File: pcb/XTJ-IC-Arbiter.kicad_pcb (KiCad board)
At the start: 2 copper layers, 80.2 x 67.8 mm, 56 parts, among them IC1 SN74LV125AN, J3 DTM13-12PA-R008, Q1 NPN, U1 LM2675N-5.0/NOPB, U2 CDP68HC68S1, U3 EEC-325X4A, U4 MCP2562-H-P, U5 SP723APP, U6 MCP1700-3302E/TO

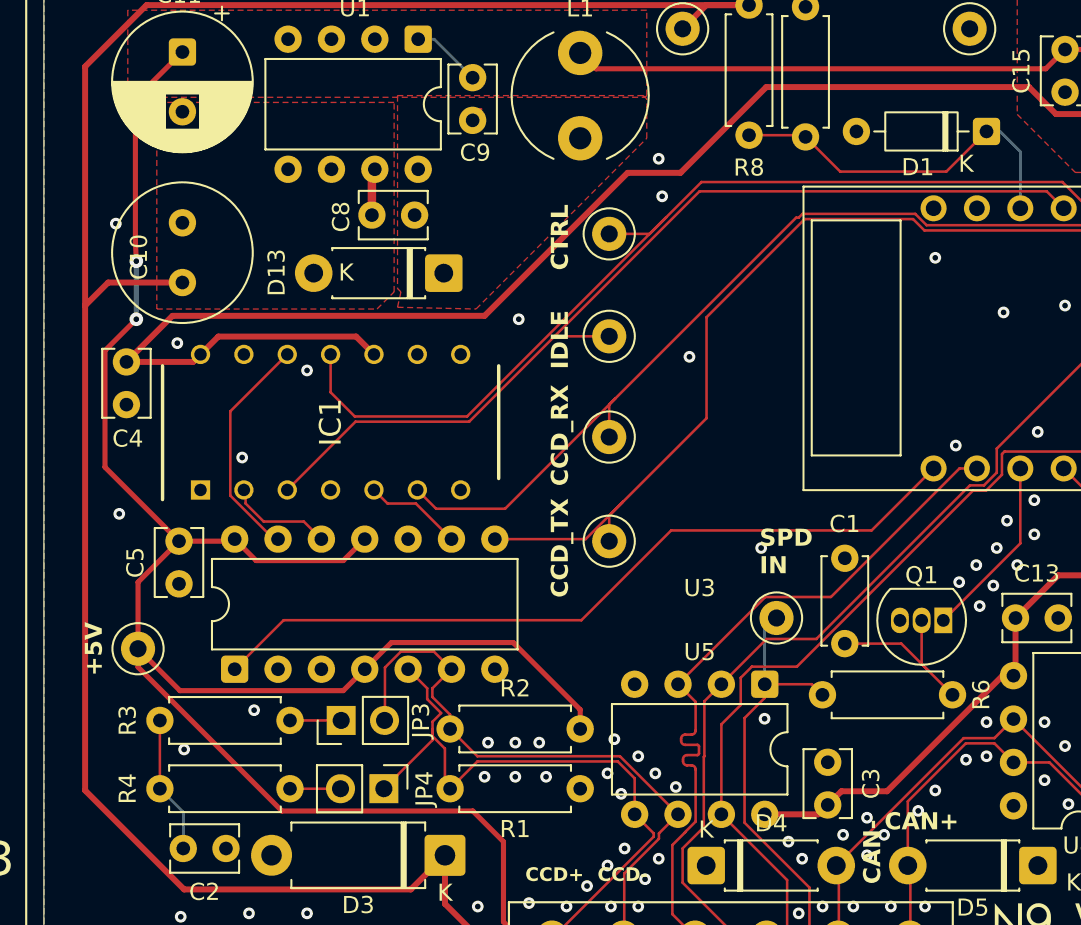
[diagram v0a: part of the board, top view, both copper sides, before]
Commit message: ensure ext I/Os are length tuned
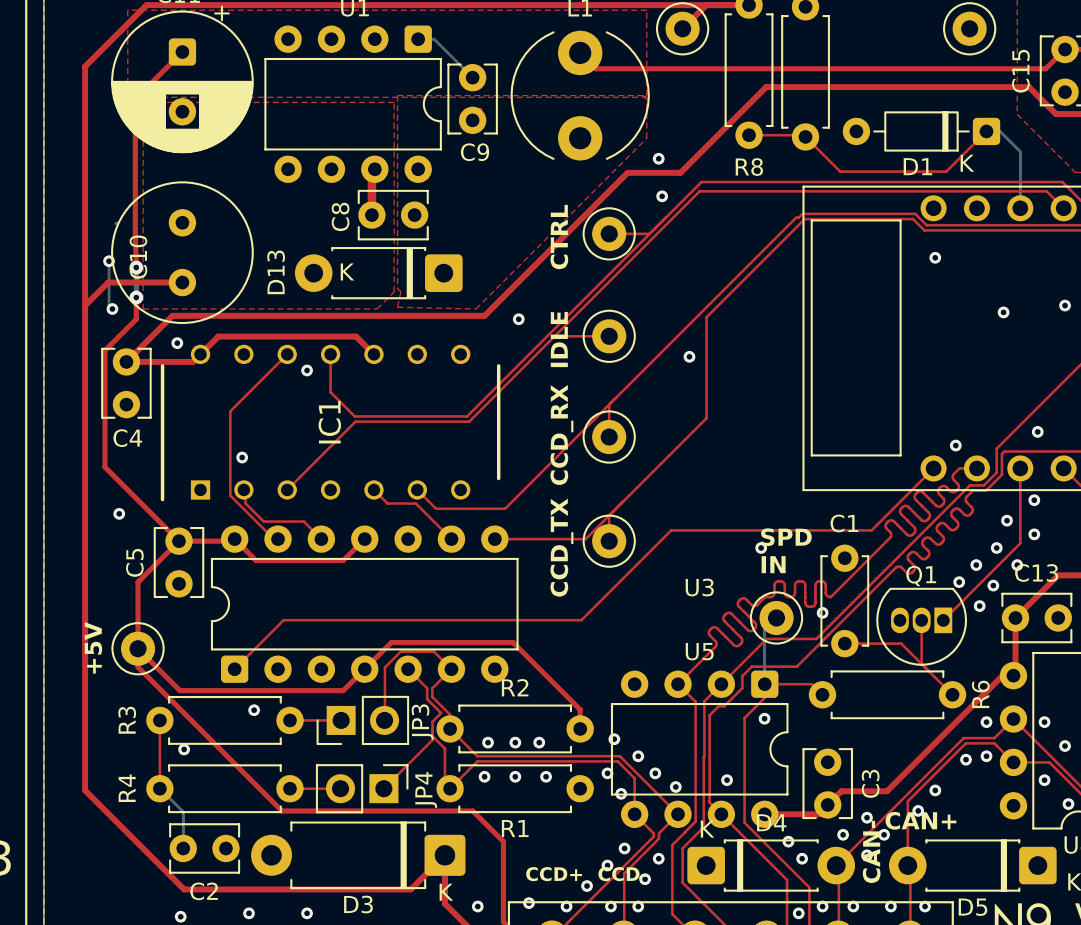
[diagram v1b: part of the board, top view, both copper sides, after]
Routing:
- net IO/1: track 41.9 -> 61.1 mm
- net IO/3: track 54.7 -> 62.0 mm
- net GND: track 0.07 -> 2.95 mm, vias 101 -> 104
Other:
- board text added: "Extended I/O pins: IO/1 -> Pin 18 IO/2 -> Pin 26 IO/3 -> Pin 4"
- board text removed: "Extended I/O pins: IO/1 -> Pin 26 IO/2 -> Pin 33 IO/3 -> Pin 18"

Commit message: After the 4 layer adventure, cleanup
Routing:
- net +5V: track 235.4 -> 235.5 mm, vias 3 -> 2
- net GND: vias 104 -> 0

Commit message: Hand tune the differential lengths (CAD/CCD)
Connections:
- net 12V_MEASURE renamed 12v_meter
- XA1 pad 13: IO/2 -> IO/1
- XA1 pad 2: IO/1 -> IO/2
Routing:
- net IO/2: track 61.4 -> 38.8 mm
- net IO/3: track 62.0 -> 55.5 mm
- net ccd-: track 36.1 -> 40.5 mm
- net +5V: track 235.5 -> 231.7 mm
- net ccd+: track 36.8 -> 39.9 mm
- net can-: track 36.1 -> 38.0 mm
- net can+: track 36.0 -> 37.7 mm
- net +3V3: track 149.2 -> 150.4 mm
- net GND: vias 0 -> 5

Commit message: silkscreen work
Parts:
- moved G*** 44.7 mm to (119.0, 121.0)
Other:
- board text added: "VOUT"
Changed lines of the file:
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@@
 	(footprint "parts:N9Works-Small"
 		(layer "F.Cu")
-		(at 163.574 117.200651)
+		(at 118.99245 121.000266)
 		(property "Reference" "G***"
 			(at 0 0 0)
@@
 	)
 	(gr_text "XJ/TJ CAN+CCD \nBus Arbiter v3.0\n"
-		(at 156 121.2 0)
+		(at 156.2 121 0)
 		(layer "F.SilkS")
 		(effects
@@
 		)
 	)
-	(gr_text "IO/1"
+	(gr_text "IO/3"
 		(at 142.646164 122.174 0)
 		(layer "B.SilkS")
@@
 		)
 	)
-	(gr_text "IO/3"
+	(gr_text "IO/1"
 		(at 138.684 116.332 0)
 		(layer "B.SilkS")
@@
 	(gr_text "CAN+"
 		(at 151.13 116.332 0)
+		(layer "B.SilkS")
+		(effects
+			(font
+				(size 1 1)
+				(thickness 0.15)
+			)
+			(justify mirror)
+		)
+	)
+	(gr_text "VOUT"
+		(at 138.6 122.2 0)
 		(layer "B.SilkS")
 		(effects
@@
 		)
 	)
+	(gr_text "+12V"
+		(at 134.8 126.6 0)
+		(layer "B.SilkS")
+		(effects
+			(font
+				(size 1 1)
+				(thickness 0.15)
+			)
+			(justify mirror)
+		)
+	)
 	(gr_text "CAN-"
 		(at 146.558 116.332 0)
@@
 	)
 	(gr_text "+5V"
-		(at 138.938 122.174 0)
+		(at 139 126.6 0)
 		(layer "B.SilkS")
 		(effects

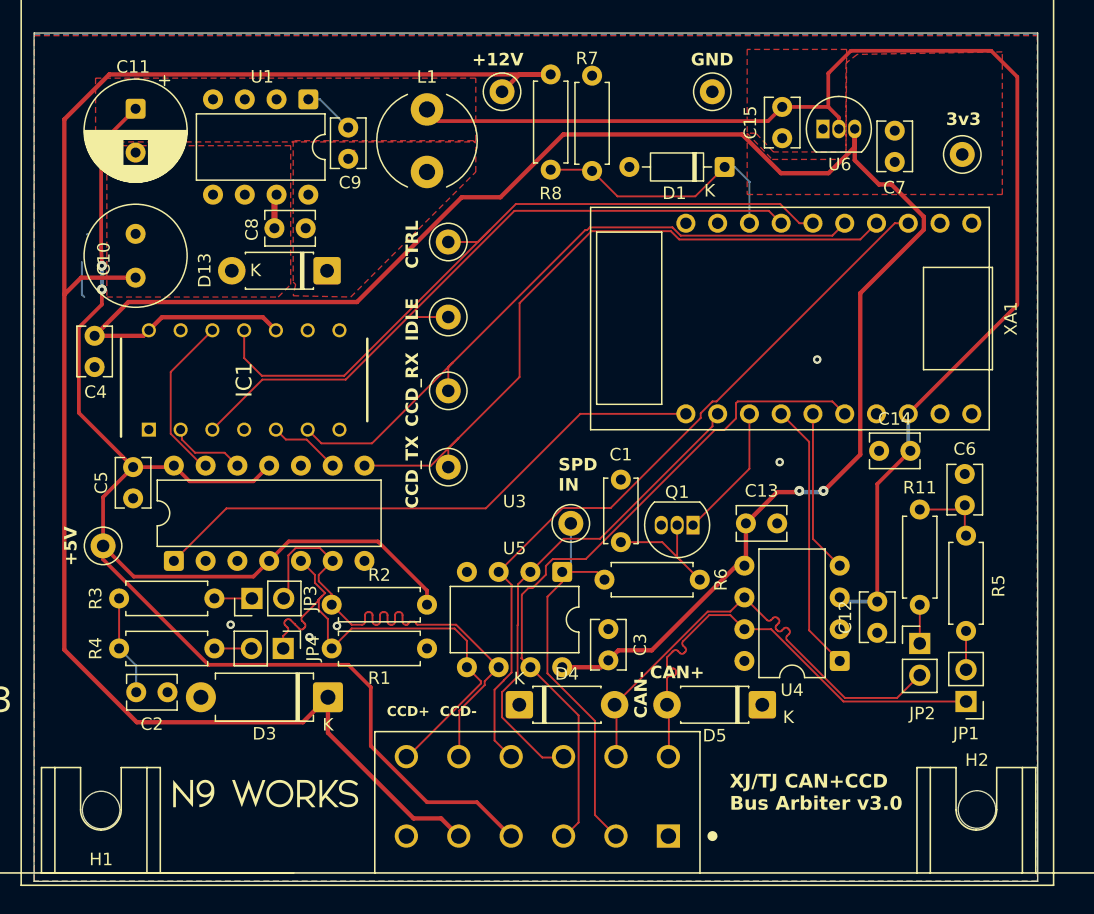
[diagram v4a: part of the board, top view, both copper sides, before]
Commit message: re-route some traces to get contiguous front ground pours without vias
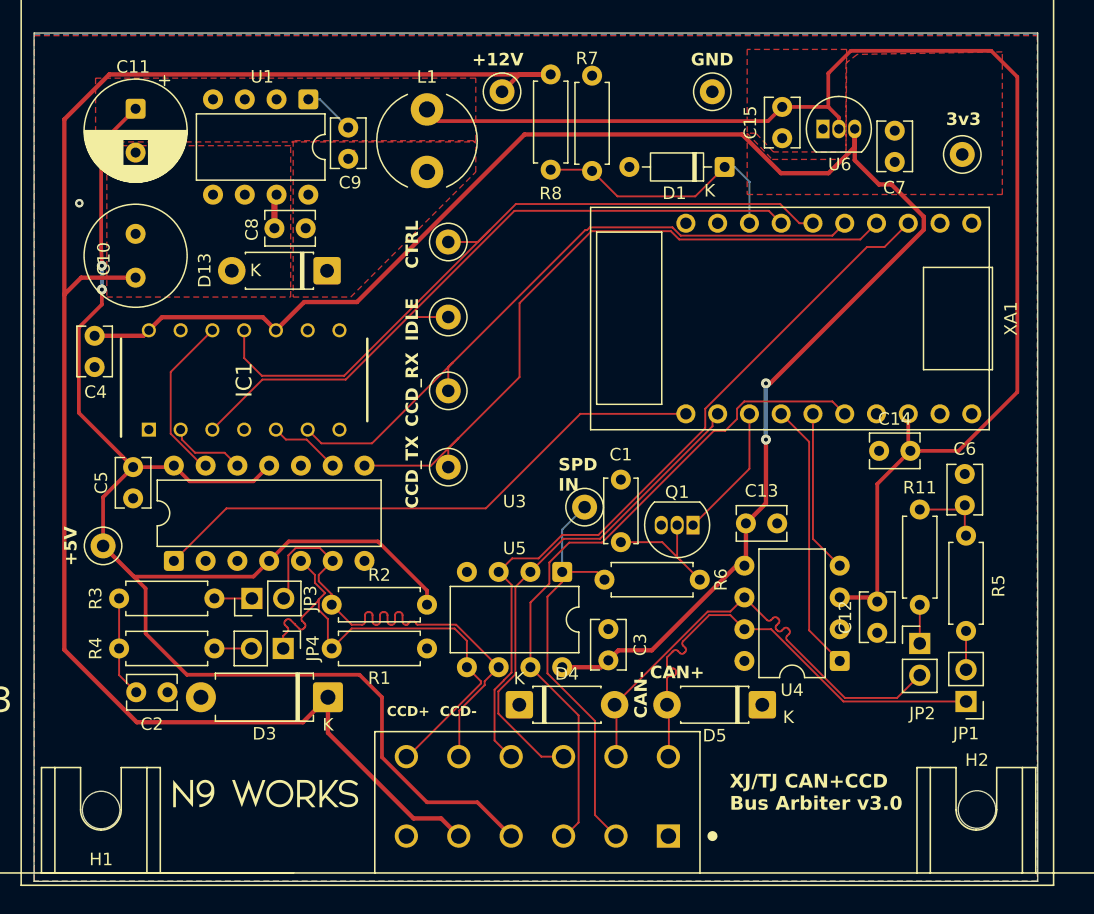
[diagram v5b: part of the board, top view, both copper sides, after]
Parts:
- moved TP1 1.70 mm to (144.6, 98.2)
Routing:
- net +3V3: track 150.4 -> 133.6 mm
- net +5V: track 231.7 -> 239.1 mm
- net GND: track 2.95 -> 0.00 mm, vias 5 -> 1
- net speedo_in: track 31.7 -> 33.4 mm
- net IO/3: track 55.5 -> 54.5 mm
- net IO/1: track 60.9 -> 61.6 mm

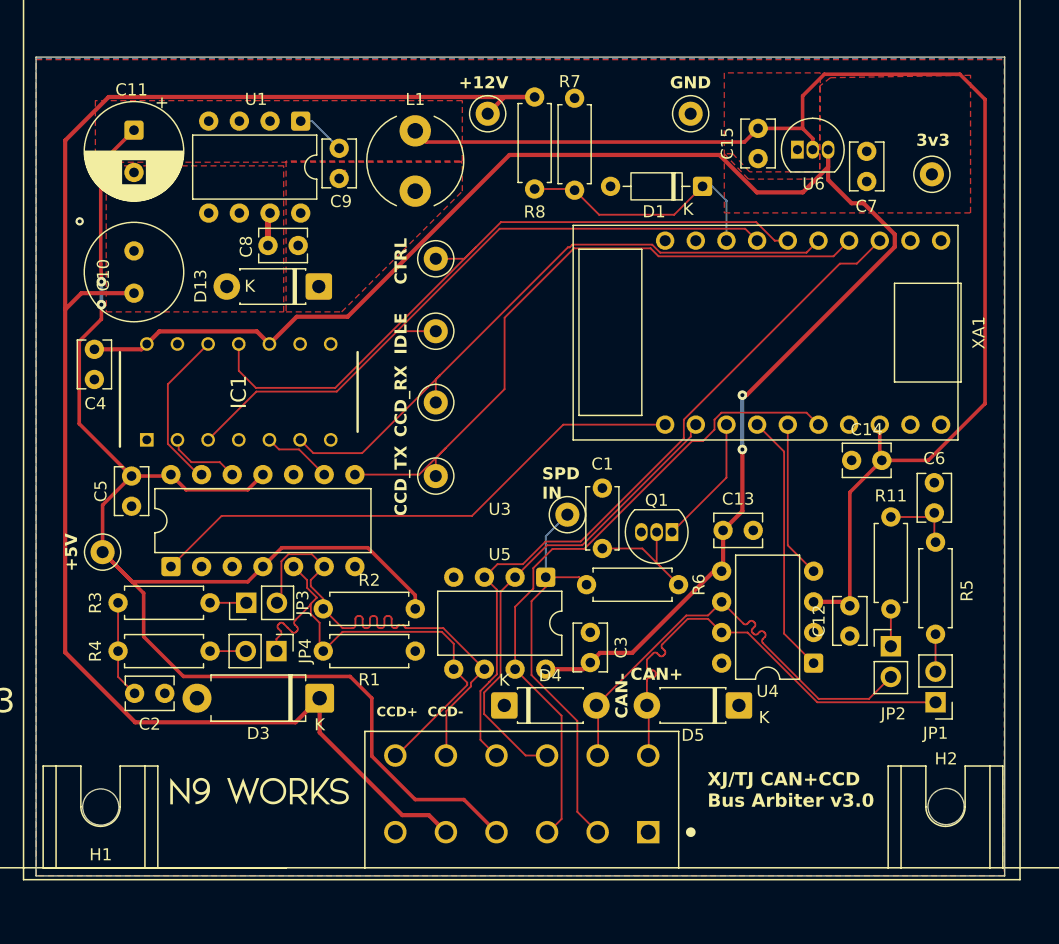
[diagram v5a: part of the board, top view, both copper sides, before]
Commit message: LDO caps were the wrong footprint
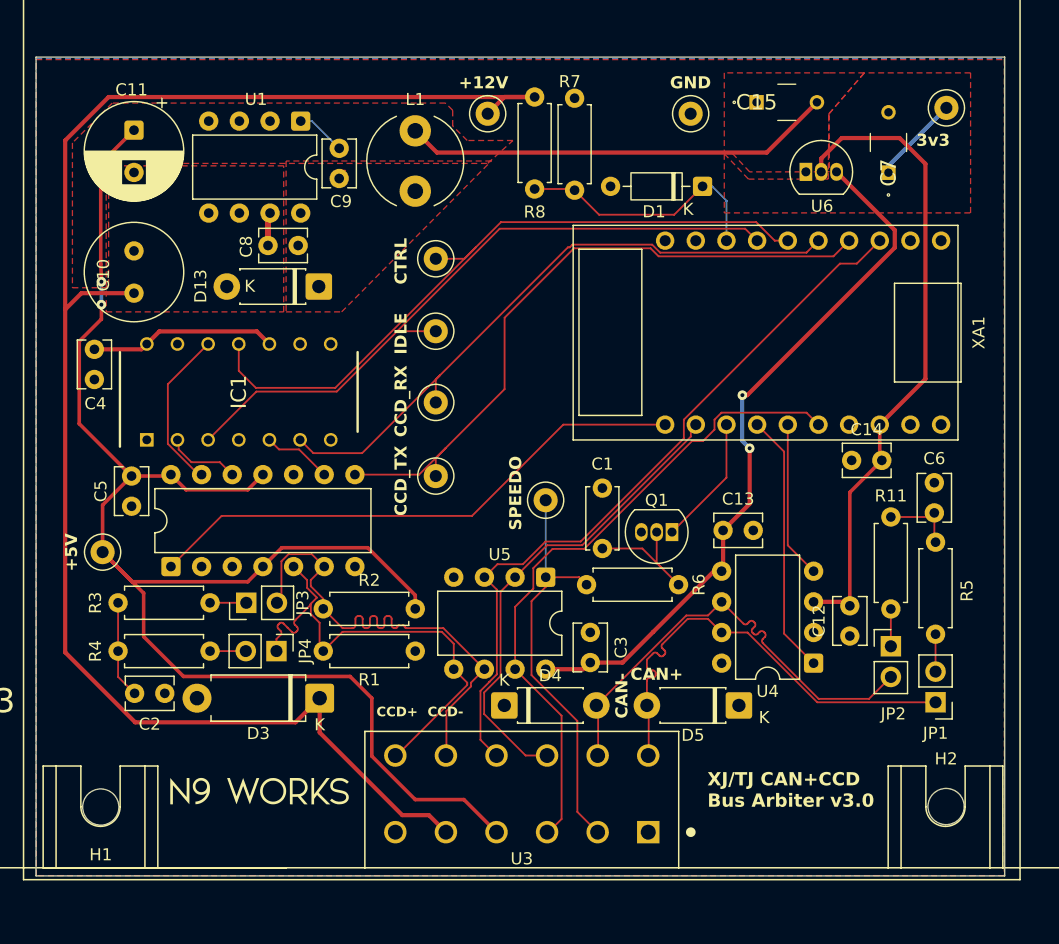
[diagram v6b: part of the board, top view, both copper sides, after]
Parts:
- C15, C7: footprint Capacitor_THT:C_Disc_D3.8mm_W2.6mm_P2.50mm -> Automotive Cap:FA24
- moved TP9 5.63 mm to (176.0, 64.5), turned to -90 degrees
- moved C15 4.66 mm to (160.3, 64.0), turned to 0 degrees
- moved C7 2.52 mm to (171.2, 69.9), turned to 90 degrees
- moved TP1 2.16 mm to (142.8, 97.0)
- moved U6 1.97 mm to (164.4, 69.8)
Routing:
- net +3V3: track 133.6 -> 82.4 mm
- net +5V: track 239.1 -> 219.1 mm
- net GND: vias 1 -> 0
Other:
- board text removed: "SPD IN"

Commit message: Other footprint fixes
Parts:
- C12, C13, C14, C3, C4, C5, C8: footprint Capacitor_THT:C_Disc_D3.8mm_W2.6mm_P2.50mm -> Capacitor_THT:C_Disc_D4.7mm_W2.5mm_P5.00mm
- moved C6 2.66 mm to (176.7, 97.6), turned to 180 degrees
- moved C13 2.40 mm to (162.4, 99.5)
- moved C5 2.30 mm to (108.6, 99.8)
- moved C3 1.97 mm to (146.2, 106.0)
- moved C1 1.75 mm to (149.0, 95.1), turned to 0 degrees
- moved TP4 0.98 mm to (105.7, 102.2)
- moved Q1 0.93 mm to (152.9, 98.8)
- moved R6 0.93 mm to (145.8, 103.2)
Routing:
- net +3V3: track 82.4 -> 140.2 mm
- net +5V: track 219.1 -> 239.0 mm
- net +12V: track 137.1 -> 134.5 mm
- net Net-(Q1-B): track 10.7 -> 9.80 mm
- net Net-(C6-Pad2): track 5.59 -> 6.38 mm
- net speedo: track 10.8 -> 10.1 mm
- net /Vsw: track 0.50 -> 0.00 mm

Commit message: colorize crucial nets
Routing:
- net +5V: track 239.0 -> 240.9 mm
- net +3V3: track 140.2 -> 139.6 mm
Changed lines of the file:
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@@
-	)
-	(segment
-		(start 170.65 93.7)
-		(end 168 96.35)
-		(width 0.3)
-		(layer "F.Cu")
-		(net 11)
 	)
 	(segment
@@
 	)
 	(segment
+		(start 110.4792 107.4)
+		(end 110.4792 106.787875)
+		(width 0.35)
+		(layer "F.Cu")
+		(net 11)
+	)
+	(segment
 		(start 178.3 82.92)
 		(end 170.48 90.74)
@@
 	)
 	(segment
-		(start 113.5 103.7808)
-		(end 118.0992 103.7808)
+		(start 110.4792 101.5)
+		(end 110.4792 107.4)
 		(width 0.35)
 		(layer "F.Cu")
@@
 	)
 	(segment
-		(start 167.67 105.42)
-		(end 168 105.75)
+		(start 110.4792 107.4)
+		(end 110.4792 107.582189)
 		(width 0.35)
 		(layer "F.Cu")
@@
 	)
 	(segment
-		(start 168 96.35)
-		(end 168 105.75)
-		(width 0.3)
-		(layer "F.Cu")
-		(net 11)
-	)
-	(segment
 		(start 176.7 61.8)
 		(end 178.3 63.4)
@@
 	)
 	(segment
+		(start 165 105.42)
+		(end 167.17 103.25)
+		(width 0.35)
+		(layer "F.Cu")
+		(net 11)
+	)
+	(segment
 		(start 167.515 61.8)
 		(end 176.7 61.8)
@@
 	)
 	(segment
-		(start 173.15 93.7)
-		(end 170.65 93.7)
-		(width 0.3)
+		(start 110.4792 103.359634)
+		(end 110.900366 103.7808)
+		(width 0.35)
+		(layer "F.Cu")
+		(net 11)
+	)
+	(segment
+		(start 118.0992 103.7808)
+		(end 119.38 102.5)
+		(width 0.35)
 		(layer "F.Cu")
 		(net 11)
@@
 	)
 	(segment
-		(start 173.15 93.41)
+		(start 170.65 93.7)
 		(end 173.15 93.7)
-		(width 0.3)
+		(width 0.35)
 		(layer "F.Cu")
 		(net 11)
@@
 	)
 	(segment
-		(start 105.7 102.2)
-		(end 107.2808 103.7808)
-		(width 0.35)
-		(layer "F.Cu")
-		(net 11)
-	)
-	(segment
 		(start 136.03 121.8)
 		(end 138.73 124.5)
@@
 	)
 	(segment
-		(start 107.2808 103.7808)
-		(end 113.5 103.7808)
-		(width 0.35)
-		(layer "F.Cu")
-		(net 11)
-	)
-	(segment
 		(start 104.1642 83.8358)
 		(end 104.1642 90.6642)
@@
 	)
 	(segment
+		(start 168 96.35)
+		(end 170.65 93.7)
+		(width 0.35)
+		(layer "F.Cu")
+		(net 11)
+	)
+	(segment
 		(start 118.1242 96.1358)
 		(end 119.38 94.88)
@@
 	)
 	(segment
+		(start 167.17 103.25)
+		(end 168 103.25)
+		(width 0.35)
+		(layer "F.Cu")
+		(net 11)
+	)
+	(segment
+		(start 168 103.25)
+		(end 168 96.35)
+		(width 0.35)
+		(layer "F.Cu")
+		(net 11)
+	)
+	(segment
 		(start 161.115 68.2)
 		(end 133.8 68.2)
@@
 	(segment
 		(start 110.4792 96.6792)
-		(end 110.4792 107.582189)
+		(end 110.4792 101.5)
 		(width 0.35)
 		(layer "F.Cu")
@@
 	)
 	(segment
-		(start 118.0992 103.7808)
-		(end 119.38 102.5)
+		(start 110.4792 101.5)
+		(end 110.4792 103.359634)
 		(width 0.35)
 		(layer "F.Cu")
@@
 	)
 	(segment
-		(start 165 105.42)
-		(end 167.67 105.42)
-		(width 0.35)
-		(layer "F.Cu")
-		(net 11)
-	)
-	(segment
 		(start 126.6 111.6)
 		(end 128.4 113.4)
@@
 	)
 	(segment
+		(start 105.891325 102.2)
+		(end 105.7 102.2)
+		(width 0.35)
+		(layer "F.Cu")
+		(net 11)
+	)
+	(segment
+		(start 110.900366 103.7808)
+		(end 118.0992 103.7808)
+		(width 0.35)
+		(layer "F.Cu")
+		(net 11)
+	)
+	(segment
 		(start 120.9416 100.9384)
 		(end 119.38 102.5)
 		(width 0.3)
+		(layer "F.Cu")
+		(net 11)
+	)
+	(segment
+		(start 110.4792 106.787875)
+		(end 105.891325 102.2)
+		(width 0.35)
 		(layer "F.Cu")
 		(net 11)
@@
 		(width 0.35)
 		(layer "F.Cu")
-		(net 13)
-	)
-	(segment
-		(start 109.76 84.06)
-		(end 109.32 84.5)
-		(width 0.35)
-		(layer "F.Cu")
